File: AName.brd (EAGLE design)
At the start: 35.2 x 24.1 mm, 10 parts, among them IC1 LM555D

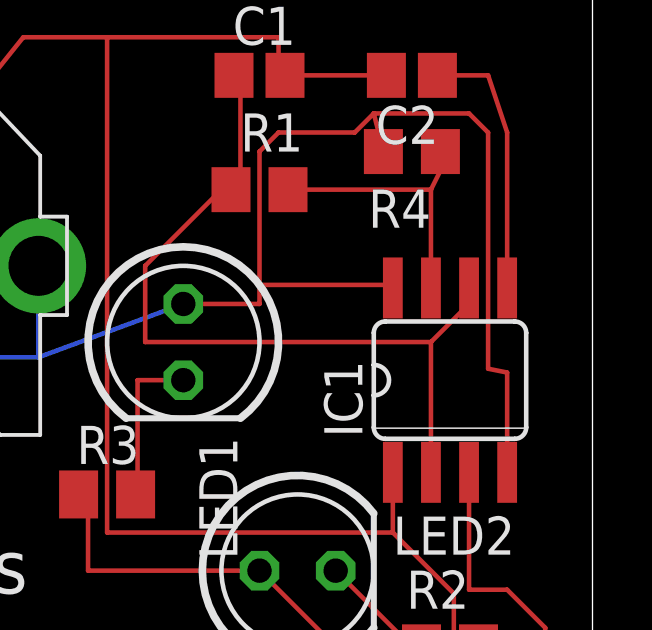
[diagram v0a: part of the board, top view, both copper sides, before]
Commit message: TH was wired to VDD. Fixed ERC errors.
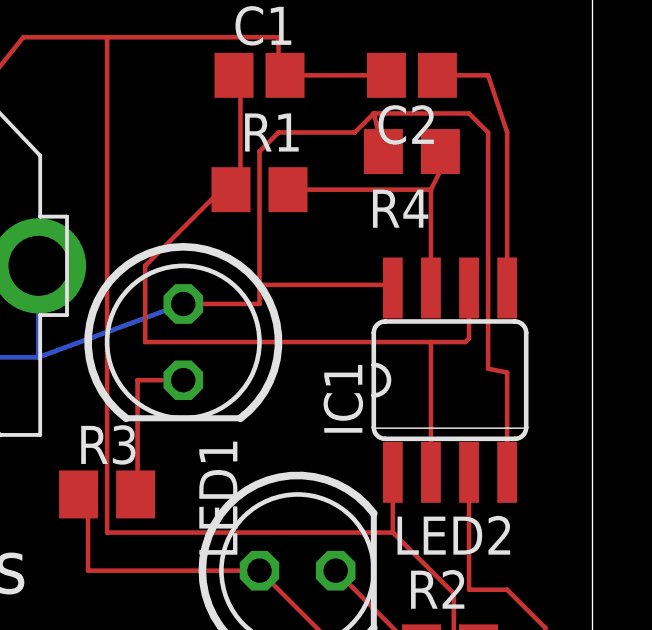
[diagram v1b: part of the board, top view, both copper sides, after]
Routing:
- net N$1: track 27.0 -> 27.7 mm
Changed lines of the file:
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@@
 <layer number="27" name="tValues" color="7" fill="1" visible="yes" active="yes"/>
 <layer number="28" name="bValues" color="7" fill="1" visible="yes" active="yes"/>
-<layer number="29" name="tStop" color="7" fill="3" visible="no" active="yes"/>
+<layer number="29" name="tStop" color="7" fill="3" visible="yes" active="yes"/>
 <layer number="30" name="bStop" color="7" fill="6" visible="no" active="yes"/>
 <layer number="31" name="tCream" color="7" fill="4" visible="no" active="yes"/>
@@
 </class>
 </classes>
-<designrules name="default">
+<designrules name="SeeedStudio_2layer_DRU_no_angle_20140221">
 <description language="de">&lt;b&gt;EAGLE Design Rules&lt;/b&gt;
 &lt;p&gt;
@@
 necessary adjustments and save your customized
 design rules under a new name.</description>
+<description language="zh">&lt;b&gt;Seeed Studio EAGLE Design Rules&lt;/b&gt;
+</description>
 <param name="layerSetup" value="(1*16)"/>
-<param name="mtCopper" value="0.035mm 0.035mm 0.035mm 0.035mm 0.035mm 0.035mm 0.035mm 0.035mm 0.035mm 0.035mm 0.035mm 0.035mm 0.035mm 0.035mm 0.035mm 0.035mm"/>
-<param name="mtIsolate" value="1.5mm 0.15mm 0.2mm 0.15mm 0.2mm 0.15mm 0.2mm 0.15mm 0.2mm 0.15mm 0.2mm 0.15mm 0.2mm 0.15mm 0.2mm"/>
+<param name="mtCopper" value="0.035mm 0.0175mm 0.035mm 0.035mm 0.035mm 0.035mm 0.035mm 0.035mm 0.035mm 0.035mm 0.035mm 0.035mm 0.035mm 0.035mm 0.0175mm 0.035mm"/>
+<param name="mtIsolate" value="1.5mm 1.1mm 0.2mm 0.15mm 0.2mm 0.15mm 0.2mm 0.15mm 0.2mm 0.15mm 0.2mm 0.15mm 0.2mm 0.15mm 0.2mm"/>
 <param name="mdWireWire" value="6mil"/>
 <param name="mdWirePad" value="6mil"/>
@@
 <param name="mdPadVia" value="6mil"/>
 <param name="mdViaVia" value="6mil"/>
-<param name="mdSmdPad" value="6mil"/>
-<param name="mdSmdVia" value="6mil"/>
-<param name="mdSmdSmd" value="6mil"/>
-<param name="mdViaViaSameLayer" value="6mil"/>
+<param name="mdSmdPad" value="0mil"/>
+<param name="mdSmdVia" value="0mil"/>
+<param name="mdSmdSmd" value="0mil"/>
+<param name="mdViaViaSameLayer" value="8mil"/>
 <param name="mnLayersViaInSmd" value="2"/>
-<param name="mdCopperDimension" value="40mil"/>
-<param name="mdDrill" value="6mil"/>
+<param name="mdCopperDimension" value="10mil"/>
+<param name="mdDrill" value="10mil"/>
 <param name="mdSmdStop" value="0mil"/>
 <param name="msWidth" value="6mil"/>
-<param name="msDrill" value="0.35mm"/>
-<param name="msMicroVia" value="9.99mm"/>
+<param name="msDrill" value="12mil"/>
+<param name="msMicroVia" value="12mil"/>
 <param name="msBlindViaRatio" value="0.5"/>
 <param name="rvPadTop" value="0.25"/>
@@
 <param name="rlMinPadBottom" value="10mil"/>
 <param name="rlMaxPadBottom" value="20mil"/>
-<param name="rlMinViaOuter" value="8mil"/>
+<param name="rlMinViaOuter" value="6mil"/>
 <param name="rlMaxViaOuter" value="20mil"/>
-<param name="rlMinViaInner" value="8mil"/>
+<param name="rlMinViaInner" value="6mil"/>
 <param name="rlMaxViaInner" value="20mil"/>
 <param name="rlMinMicroViaOuter" value="4mil"/>
@@
 <param name="psTop" value="-1"/>
 <param name="psBottom" value="-1"/>
-<param name="psFirst" value="-1"/>
+<param name="psFirst" value="0"/>
 <param name="psElongationLong" value="100"/>
 <param name="psElongationOffset" value="100"/>
 <param name="mvStopFrame" value="1"/>
 <param name="mvCreamFrame" value="0"/>
-<param name="mlMinStopFrame" value="4mil"/>
-<param name="mlMaxStopFrame" value="4mil"/>
+<param name="mlMinStopFrame" value="2mil"/>
+<param name="mlMaxStopFrame" value="2mil"/>
 <param name="mlMinCreamFrame" value="0mil"/>
 <param name="mlMaxCreamFrame" value="0mil"/>
-<param name="mlViaStopLimit" value="0mil"/>
+<param name="mlViaStopLimit" value="100mil"/>
 <param name="srRoundness" value="0"/>
 <param name="srMinRoundness" value="0mil"/>
@@
 <param name="checkAngle" value="0"/>
 <param name="checkFont" value="1"/>
-<param name="checkRestrict" value="1"/>
+<param name="checkRestrict" value="0"/>
 <param name="checkStop" value="0"/>
 <param name="checkValues" value="0"/>
@@
 <contactref element="C1" pad="1"/>
 <contactref element="IC1" pad="2"/>
-<contactref element="IC1" pad="6"/>
 <contactref element="R1" pad="1"/>
 <wire x1="24.765" y1="22.86" x2="24.765" y2="19.05" width="0.1524" layer="1"/>
@@
 <wire x1="24.765" y1="22.86" x2="24.55" y2="22.86" width="0.1524" layer="1"/>
 <wire x1="31.115" y1="13.97" x2="31.115" y2="9.6266" width="0.1524" layer="1"/>
-<wire x1="32.385" y1="15.24" x2="31.115" y2="13.97" width="0.1524" layer="1"/>
-<wire x1="32.385" y1="15.24" x2="32.385" y2="15.7734" width="0.1524" layer="1"/>
 <wire x1="21.59" y1="16.51" x2="24.13" y2="19.05" width="0.1524" layer="1"/>
 <wire x1="21.59" y1="13.97" x2="21.59" y2="16.51" width="0.1524" layer="1"/>
 <wire x1="31.115" y1="13.97" x2="21.59" y2="13.97" width="0.1524" layer="1"/>
 <wire x1="24.13" y1="19.05" x2="24.45" y2="19.05" width="0.1524" layer="1"/>
+<contactref element="IC1" pad="6"/>
+<wire x1="32.385" y1="15.7734" x2="32.385" y2="14.097" width="0.1524" layer="1"/>
+<wire x1="32.385" y1="14.097" x2="32.258" y2="13.97" width="0.1524" layer="1"/>
+<wire x1="32.258" y1="13.97" x2="31.115" y2="13.97" width="0.1524" layer="1"/>
 </signal>
 <signal name="N$2">
